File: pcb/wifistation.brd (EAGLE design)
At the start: 74.6 x 41.9 mm, 6 parts

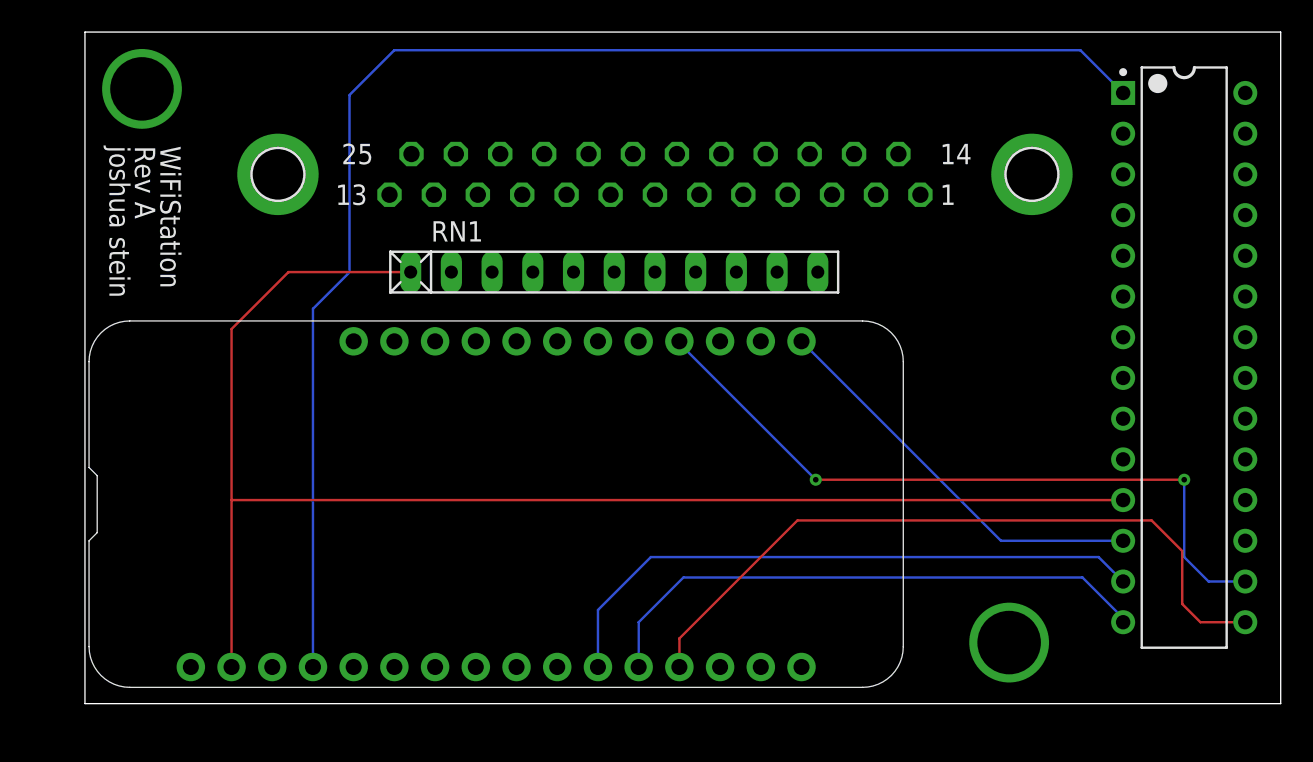
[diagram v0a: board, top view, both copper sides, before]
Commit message: pcb: Add revision B, which fixes the pinout of the DB25 connector
The pinout of the d-sub part in Eagle was backwards from how I was
using it :(
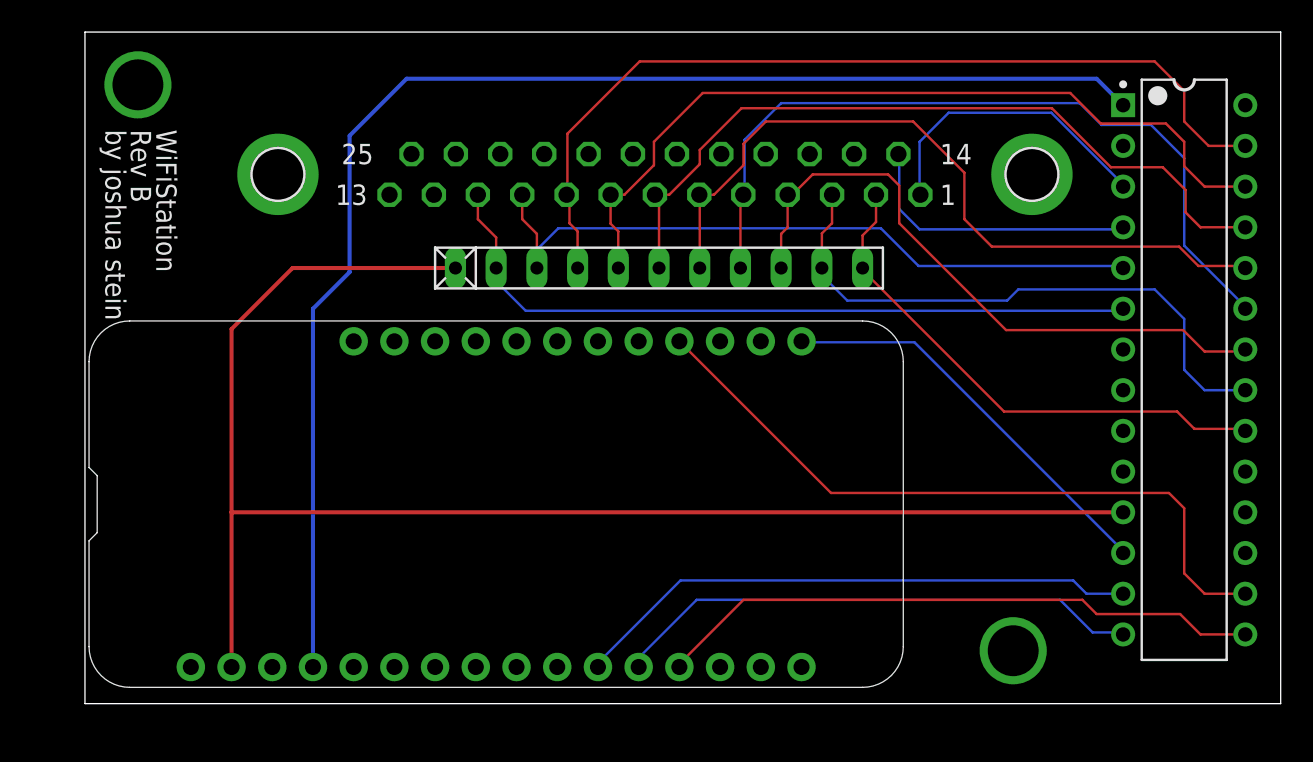
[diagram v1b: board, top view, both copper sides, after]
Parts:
- H1, H2: value SPECIAL_DRILL_0.1560 -> SPECIAL_DRILL_0.1250; device special-drill:PAD_0.1560 -> special-drill:PAD_0.1250
- moved RN1 2.81 mm to (35.8, 66.5)
- moved 1 0.76 mm to (68.6, 60.2)
- moved H2 0.57 mm to (57.9, 42.7)
- moved H1 0.36 mm to (3.30, 78.0)
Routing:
- net DATA7: track 0.00 -> 56.1 mm
- net DATA6: track 0.00 -> 51.2 mm
- net DATA3: track 0.00 -> 49.1 mm
- net DATA5: track 0.00 -> 48.2 mm
- net DATA4: track 0.00 -> 46.9 mm
- net BUSY: track 0.00 -> 45.8 mm
- net ACK: track 0.00 -> 44.3 mm
- net DATA2: track 0.00 -> 39.8 mm
- net DATA1: track 0.00 -> 37.2 mm
- net DATA0: track 0.00 -> 33.1 mm
- net STROBE: track 0.00 -> 18.9 mm
- net LINEFEED: track 0.00 -> 18.0 mm
- net N$2: track 45.1 -> 38.0 mm
- net 3V: track 89.4 -> 92.3 mm
- net N$1: track 87.2 -> 84.5 mm
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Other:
- board text added: "WiFiStation Rev B by joshua stein"
- board text removed: "WiFiStation Rev A joshua stein"

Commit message: pcb: Add revision C which grounds the DB25 mounts and pins 18-25
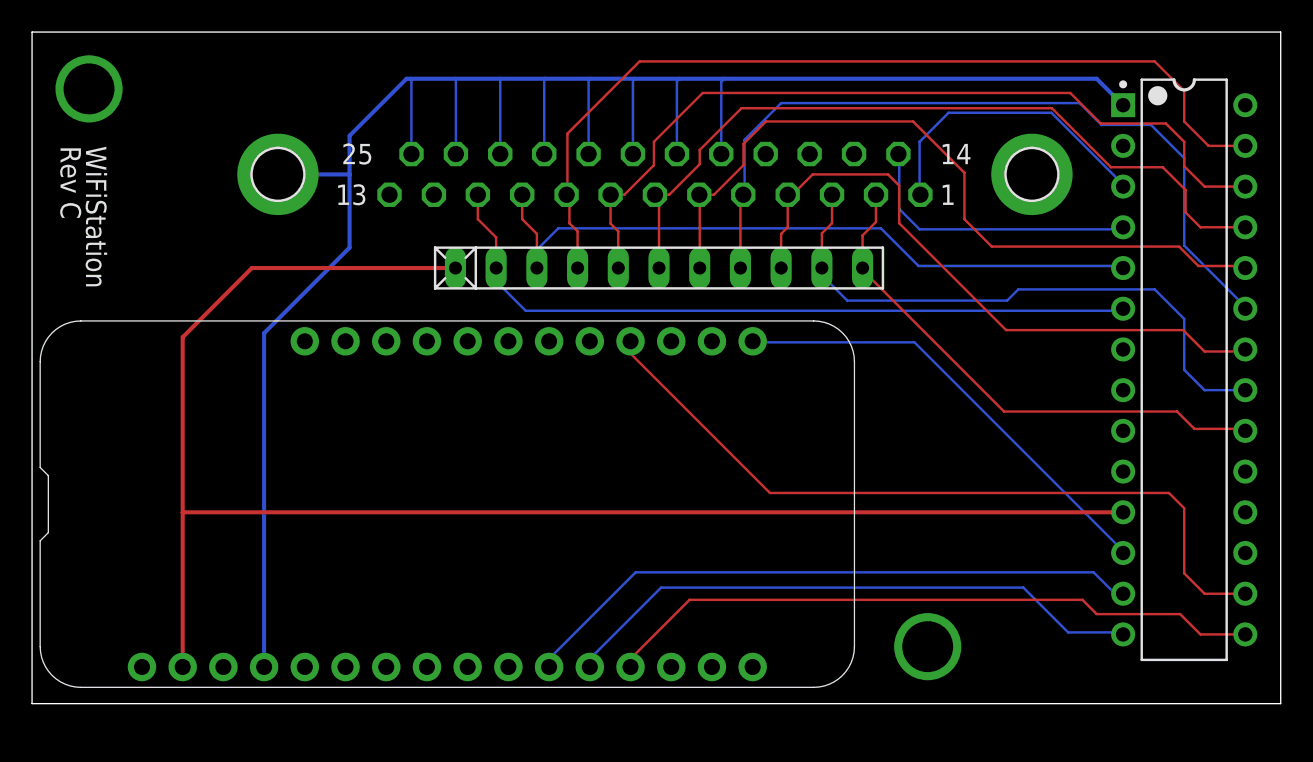
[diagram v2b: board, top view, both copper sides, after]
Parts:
- moved H2 5.34 mm to (52.6, 42.9)
- moved H1 3.06 mm to (0.25, 77.7)
- moved FEATHER 3.05 mm to (-2.79, 40.4)
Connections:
- net N$1: now also DB25.18, DB25.19, DB25.20, DB25.21, DB25.22, DB25.23, DB25.24, DB25.25, DB25.G1
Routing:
- net N$1: track 84.5 -> 128.1 mm
- net 3V: track 92.3 -> 98.1 mm
- net N$5: track 35.8 -> 39.4 mm
- net N$3: track 44.3 -> 47.8 mm
- net N$2: track 38.0 -> 41.3 mm
- net N$6: track 25.6 -> 28.7 mm
- net N$4: track 33.5 -> 36.4 mm
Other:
- board size 74.6 x 41.9 mm -> 77.9 x 41.9 mm
- board text added: "WiFiStation Rev C"
- board text removed: "WiFiStation Rev B by joshua stein"

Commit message: pcb: Add Revision D of board, much smaller now
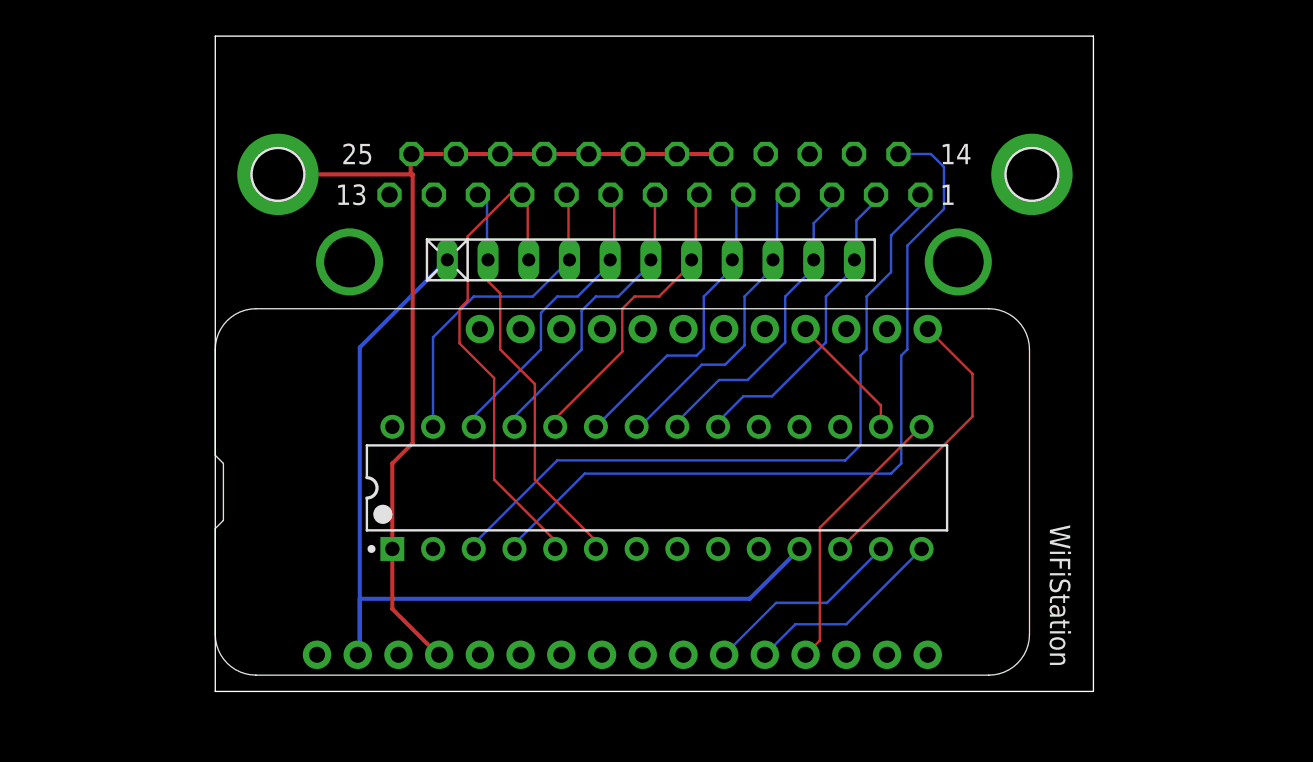
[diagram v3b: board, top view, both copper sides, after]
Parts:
- moved H1 55.3 mm to (54.5, 66.9)
- moved H2 43.3 mm to (16.5, 66.9)
- moved 1 33.7 mm to (35.7, 52.8), turned to 90 degrees
- moved FEATHER 10.9 mm to (8.13, 41.1)
- moved RN1 0.72 mm to (35.3, 67.1)
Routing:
- net N$1: track 128.1 -> 60.8 mm
- net N$3: track 47.8 -> 8.16 mm
- net 3V: track 98.1 -> 59.2 mm
- net DATA7: track 56.1 -> 20.3 mm
- net DATA6: track 51.2 -> 19.1 mm
- net LINEFEED: track 18.0 -> 49.4 mm
- net DATA5: track 48.2 -> 18.9 mm
- net DATA3: track 49.1 -> 20.0 mm
- net DATA4: track 46.9 -> 19.2 mm
- net N$5: track 39.4 -> 12.8 mm
- net STROBE: track 18.9 -> 44.2 mm
- net N$2: track 41.3 -> 17.3 mm
- net N$4: track 36.4 -> 12.5 mm
- net BUSY: track 45.8 -> 25.6 mm
- net DATA2: track 39.8 -> 19.7 mm
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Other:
- board size 77.9 x 41.9 mm -> 54.8 x 40.9 mm
- board text added: "WiFiStation"
- board text removed: "WiFiStation Rev C"
